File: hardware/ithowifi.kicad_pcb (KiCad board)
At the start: 2 copper layers, 42.3 x 49.5 mm, 8 parts, among them J1 conn

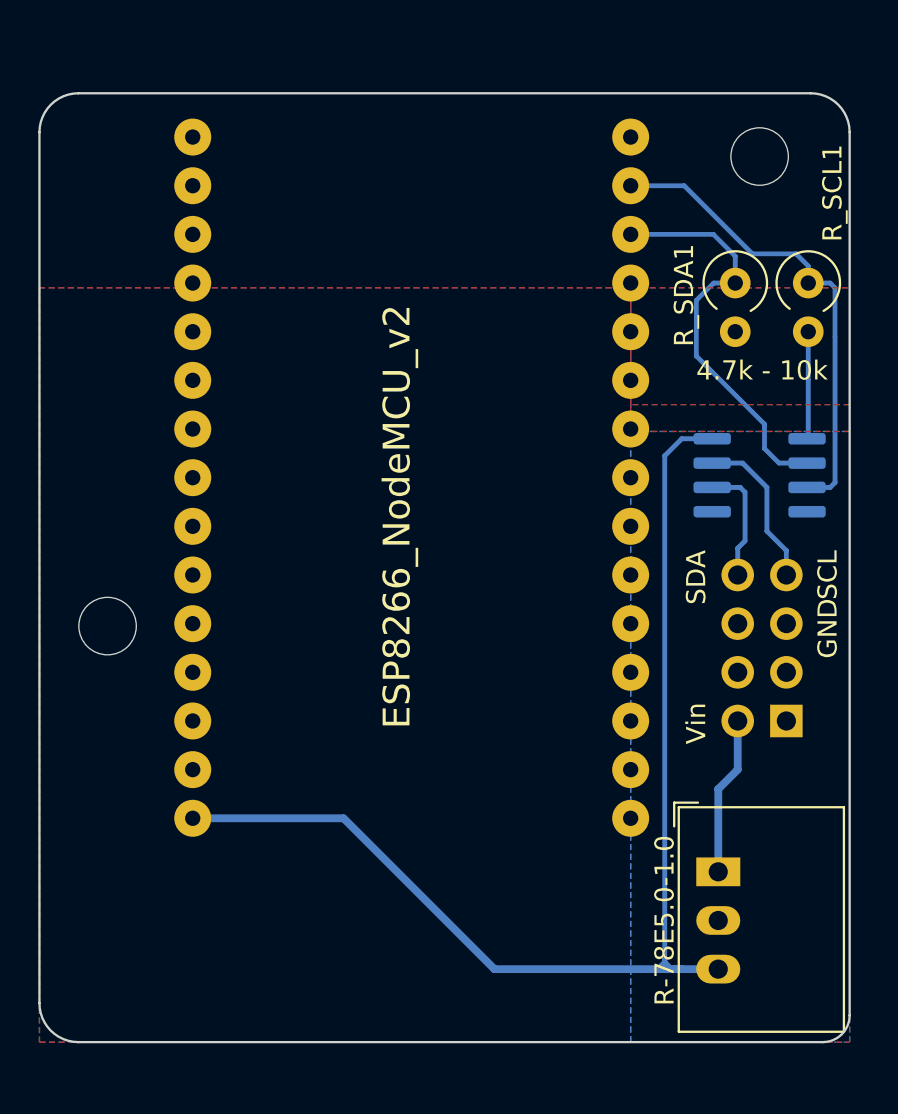
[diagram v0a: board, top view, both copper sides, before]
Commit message: Updated PCB to version 1.1, added more advanced firmware - PCB version 1.0 wasn't working properly, updated version 1.1 is tested and works - Uploaded a more advanced, 'field' configurable firmware and OTA support - Added images of the add-on - Updated readme
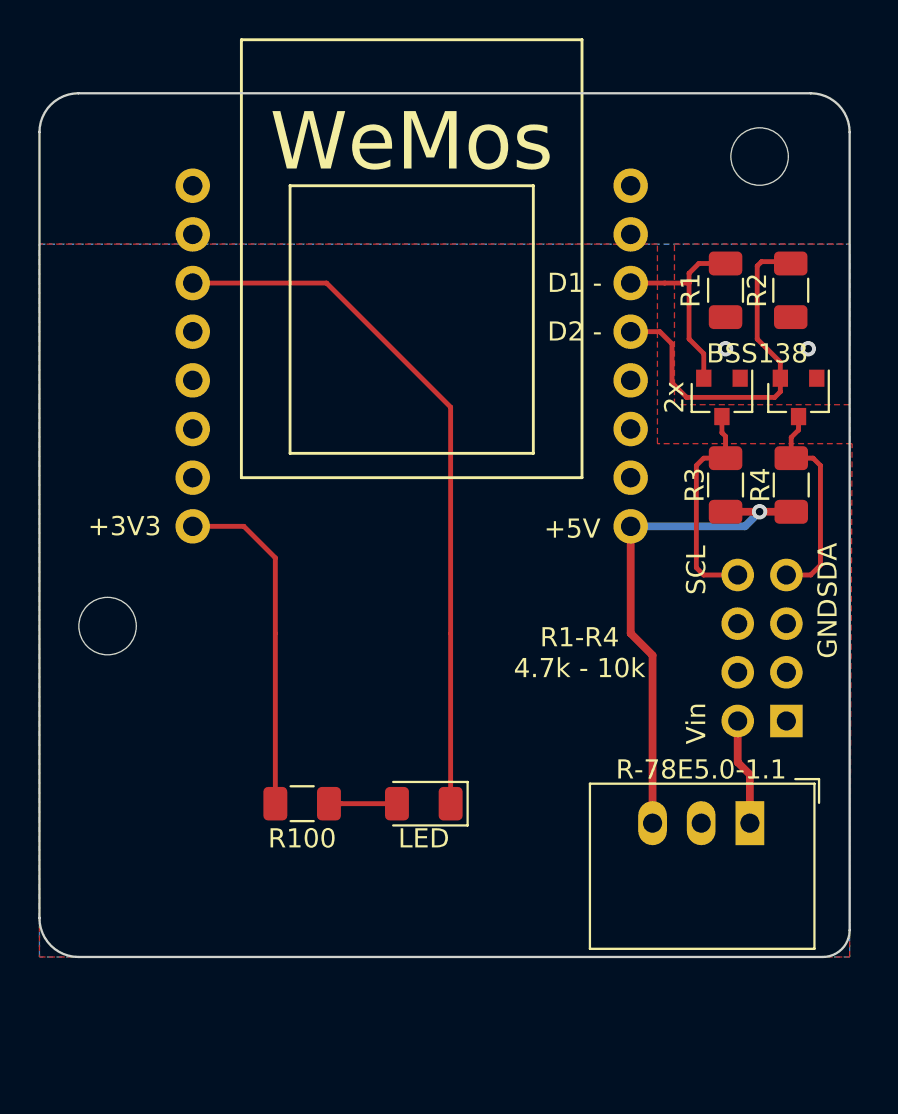
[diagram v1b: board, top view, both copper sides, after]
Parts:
- removed ESP8266_NodeMCU_v2: U1, MCU_NodeMCU:ESP12E_DEVKIT
- removed ISO1540: U3, Package_SO:SOIC-8_3.9x4.9mm_P1.27mm
- removed R-78E5.0-1.0: U2, Converter_DCDC:Converter_DCDC_RECOM_R-78E-0.5_THT
- removed R_SCL1, R_SDA1: R4.7K, Resistor_THT:R_Axial_DIN0309_L9.0mm_D3.2mm_P2.54mm_Vertical
- added 2x: BSS138, Package_TO_SOT_SMD:SOT-23, F.Cu at (118.7, 120.9)
- added BSS138: BSS138, Package_TO_SOT_SMD:SOT-23, F.Cu at (122.7, 120.9)
- added LED: LED, LED_SMD:LED_1206_3216Metric, F.Cu at (103.1, 142.1)
- added R-78E5.0-1.1: U2, Converter_DCDC:Converter_DCDC_RECOM_R-78E-0.5_THT, F.Cu at (120.1, 143.1)
- added R1: R4.7K, Resistor_SMD:R_1206_3216Metric, F.Cu at (118.9, 115.3)
- added R100: R100, Resistor_SMD:R_1206_3216Metric, F.Cu at (96.8, 142.1)
- added R2: R4.7K, Resistor_SMD:R_1206_3216Metric, F.Cu at (122.3, 115.3)
- added R3: R4.7K, Resistor_SMD:R_1206_3216Metric, F.Cu at (118.9, 125.5)
- added R4: R4.7K, Resistor_SMD:R_1206_3216Metric, F.Cu at (122.3, 125.5)
- added U1: WeMos_mini, wemos_d1_mini:D1_mini_board, B.Cu at (102.5, 120.0)
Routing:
- net Net-(D1-Pad1): track 0.00 -> 36.8 mm
- net +5V: track 61.8 -> 26.4 mm, vias 0 -> 1
- net Net-(ESP8266_NodeMCU_v2-PadD1): track 25.1 -> 0.00 mm
- net Net-(ESP8266_NodeMCU_v2-PadD2): track 21.5 -> 0.00 mm
- net Net-(Q1-Pad2): track 0.00 -> 19.5 mm
- net +3V3: track 5.61 -> 17.8 mm, vias 0 -> 2
- net Net-(Q2-Pad2): track 0.00 -> 11.0 mm
- net Net-(J1-Pad8): track 6.42 -> 11.6 mm
- net Net-(D1-Pad2): track 0.00 -> 3.55 mm
- net Net-(J1-Pad7): track 8.50 -> 11.2 mm
- net +16V3: track 8.17 -> 5.60 mm
- net GND: track 0.80 -> 0.00 mm
- removed copper zone on B.Cu, net GND
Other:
- board size 42.3 x 49.5 mm -> 42.3 x 45.1 mm
- board text added: "+3V3"
- board text added: "+5V"
- board text added: "D1 -"
- board text added: "D2 -"
- board text added: "Itho CVE ESP WiFi Controller v1.1 Arjen Hiemstra GNU General Public License 3.0 github.com/arjenhiemstra/ithowifi"
- board text added: "R1-R4 4.7k - 10k"
- board text removed: "4.7k - 10k"
- board text removed: "Itho CVE ESP WiFi Controller v1.0 Arjen Hiemstra GNU General Public License 3.0 github.com/arjenhiemstra/ithowifi"

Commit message: Release 1.2
- Updated PCB design to accommodate a ATTiny 1614 to handle the I2C init with the itho box (Wemos often boots too slow to handle this reliable)
- Added firmware for the ATTiny
- Updated Wemos and basic firmware to work with the ATTiny 1614
- Improved WiFi stability
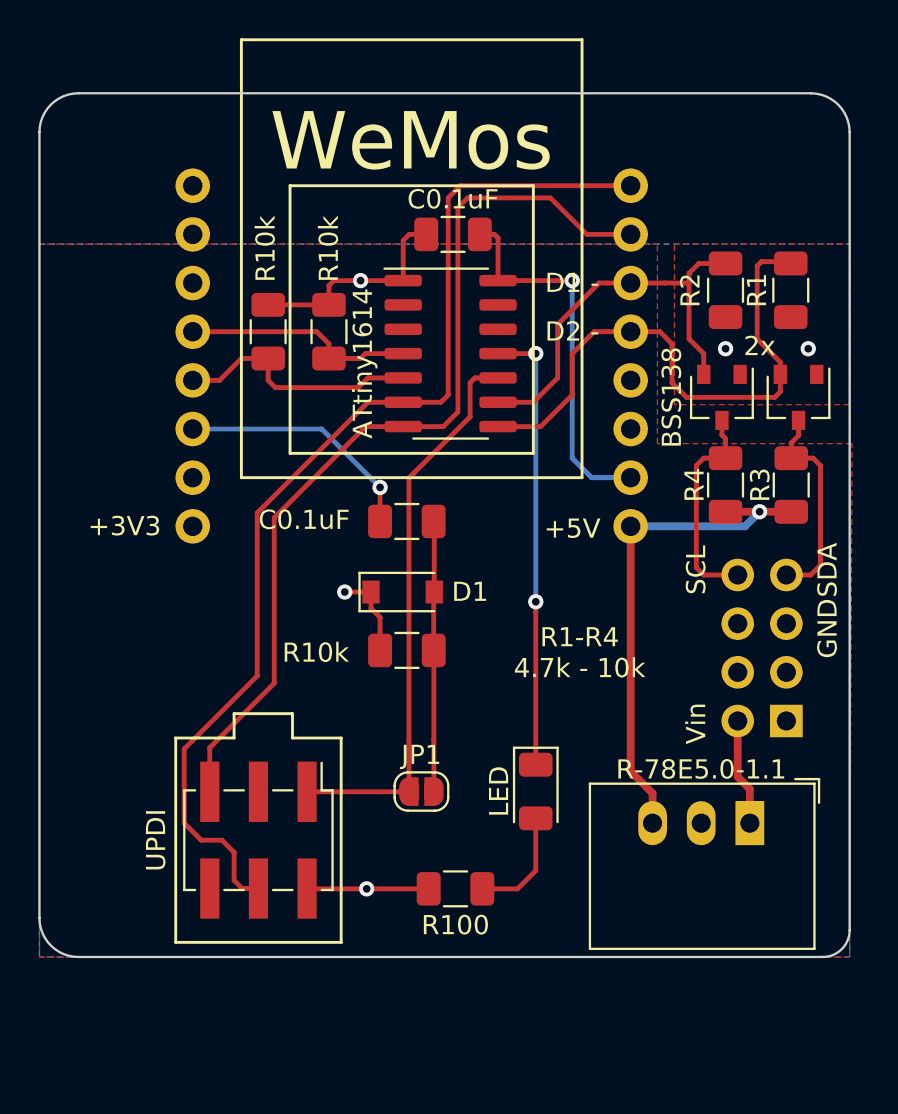
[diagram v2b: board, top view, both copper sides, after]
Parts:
- removed  : 3mm, MountingHole:MountingHole_3mm (x2)
- added ATtiny1614: ATtiny1614-SS, Package_SO:SOIC-14_3.9x8.7mm_P1.27mm, F.Cu at (104.5, 118.6)
- added C0.1uF: 0.1uF, Inductor_SMD:L_1206_3216Metric, F.Cu at (104.6, 112.4)
- added C0.1uF: C0.1uF, Inductor_SMD:L_1206_3216Metric, F.Cu at (102.2, 127.4)
- added D1: D, Diode_SMD:D_SOD-123, F.Cu at (102.0, 131.1)
- added JP1: SolderJumper_2_Open, Jumper:SolderJumper-2_P1.3mm_Open_RoundedPad1.0x1.5mm, F.Cu at (103.0, 141.5)
- added R10k: R10K, Resistor_SMD:R_1206_3216Metric, F.Cu at (95.0, 117.5)
- added R10k: R10K, Resistor_SMD:R_1206_3216Metric, F.Cu at (98.2, 117.5)
- added R10k: R10K, Resistor_SMD:R_1206_3216Metric, F.Cu at (102.2, 134.1)
- added UPDI: Conn_02x03_Odd_Even, Connector_PinHeader_2.54mm:PinHeader_2x03_P2.54mm_Vertical_SMD, F.Cu at (94.5, 144.0)
- 2x: renamed from BSS138; footprint Package_TO_SOT_SMD:SOT-23 -> Package_TO_SOT_SMD:SOT-23W
- BSS138: renamed from 2x; footprint Package_TO_SOT_SMD:SOT-23 -> Package_TO_SOT_SMD:SOT-23W
- R1: renamed from R2; value R4.7K -> R10K
- R2: renamed from R1; value R4.7K -> R10K
- R3: renamed from R4; value R4.7K -> R10K
- R4: renamed from R3; value R4.7K -> R10K
- moved R100 9.16 mm to (104.8, 146.6), turned to 0 degrees
- moved LED 5.88 mm to (109.0, 141.5), turned to 270 degrees
- renumbered J1 to J2
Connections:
- net Net-(J1-Pad7) renamed SDA
- net Net-(J1-Pad8) renamed SCL
- LED pad 1: Net-(D1-Pad1) -> Net-(ATtiny1614-Pad11)
- LED pad 2: Net-(D1-Pad2) -> Net-(R100-Pad2)
- R100 pad 1: Net-(D1-Pad2) -> +3V3
- R100 pad 2: +3V3 -> Net-(R100-Pad2)
- U1 pad 11: Net-(D1-Pad1) -> Net-(U1-Pad11)
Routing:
- net Net-(ATtiny1614-Pad6): track 0.00 -> 56.5 mm
- net Net-(ATtiny1614-Pad7): track 0.00 -> 48.3 mm
- net Net-(D1-Pad1): track 36.8 -> 0.00 mm
- net Net-(ATtiny1614-Pad10): track 0.00 -> 29.9 mm
- net Net-(ATtiny1614-Pad11): track 0.00 -> 23.4 mm, vias 0 -> 2
- net GND: track 0.00 -> 19.9 mm, vias 0 -> 1
- net Net-(C0.1uF1-Pad2): track 0.00 -> 14.1 mm
- net Net-(ATtiny1614-Pad5): track 0.00 -> 13.0 mm
- net Net-(C0.1uF1-Pad1): track 0.00 -> 12.8 mm, vias 0 -> 1
- net Net-(ATtiny1614-Pad4): track 0.00 -> 12.1 mm
- net Net-(ATtiny1614-Pad9): track 11.0 -> 22.1 mm
- net Net-(ATtiny1614-Pad8): track 19.5 -> 29.7 mm
- net Net-(R100-Pad2): track 0.00 -> 5.91 mm
- net +3V3: track 17.8 -> 22.6 mm, vias 2 -> 5
- net Net-(D1-Pad2): track 3.55 -> 0.00 mm
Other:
- board text added: "Itho CVE ESP WiFi Controller v1.2 Arjen Hiemstra GNU General Public License 3.0 github.com/arjenhiemstra/ithowifi"
- board text removed: "Itho CVE ESP WiFi Controller v1.1 Arjen Hiemstra GNU General Public License 3.0 github.com/arjenhiemstra/ithowifi"

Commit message: Version 2.0.3
- Support for hardware revision 2
- Experimental itho RF remote support
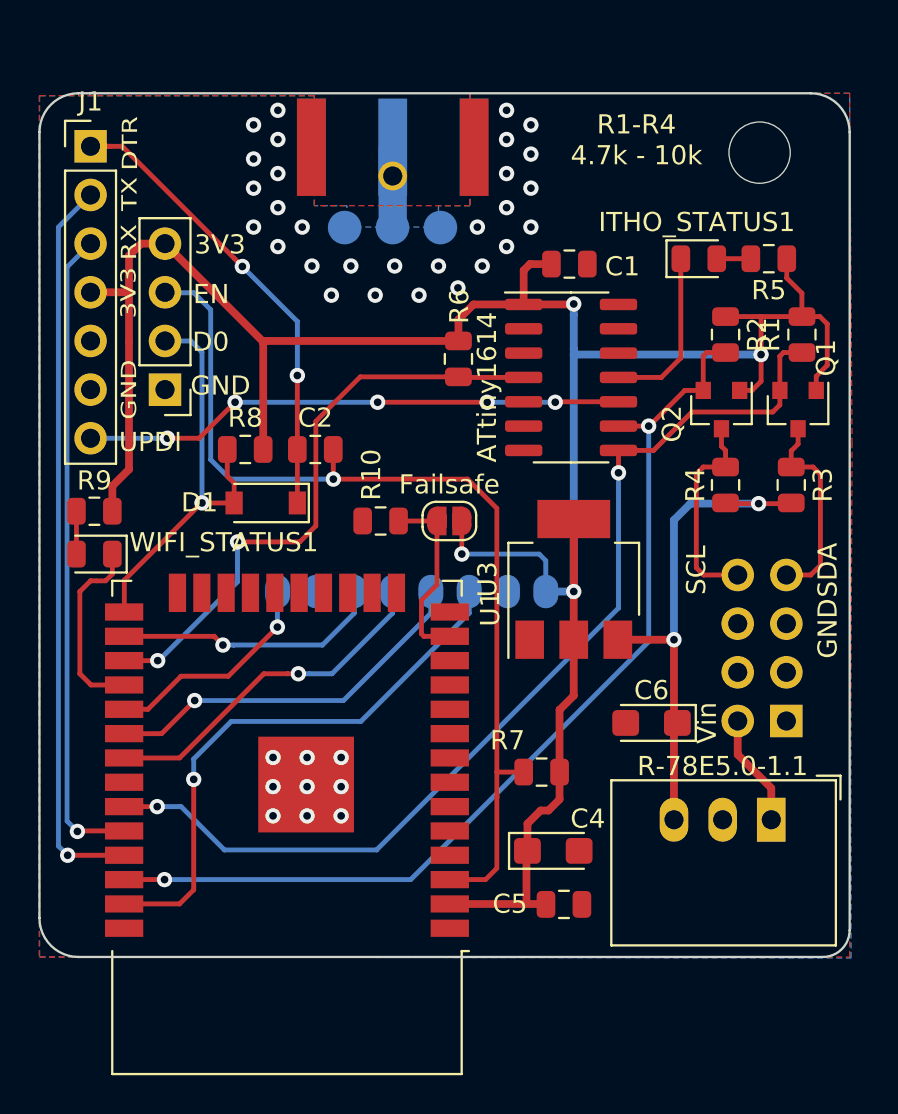
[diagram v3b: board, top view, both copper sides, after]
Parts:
- removed C0.1uF: 0.1uF, Inductor_SMD:L_1206_3216Metric
- removed C0.1uF: C0.1uF, Inductor_SMD:L_1206_3216Metric
- removed LED: LED, LED_SMD:LED_1206_3216Metric
- removed R10k (x3): R10K, Resistor_SMD:R_1206_3216Metric
- removed UPDI: Conn_02x03_Odd_Even, Connector_PinHeader_2.54mm:PinHeader_2x03_P2.54mm_Vertical_SMD
- added C1: 0,1uF, Inductor_SMD:L_0805_2012Metric, F.Cu at (110.7, 113.9)
- added C2: 1uF, Capacitor_SMD:C_0805_2012Metric, F.Cu at (97.5, 123.6)
- added C4: 10uF, Capacitor_Tantalum_SMD:CP_EIA-3216-12_Kemet-S, F.Cu at (109.9, 144.6)
- added C5: 0.1uF, Capacitor_SMD:C_0805_2012Metric, F.Cu at (110.4, 147.4)
- added C6: 10uF, Capacitor_Tantalum_SMD:CP_EIA-3216-12_Kemet-S, F.Cu at (115.0, 137.9)
- added H1: MountingHole, MountingHole:MountingHole_2.5mm, F.Cu at (120.7, 108.1)
- added ITHO_STATUS1: LED, LED_SMD:LED_0805_2012Metric, F.Cu at (117.5, 113.7)
- added J1: CONN_01X07, Connector_PinHeader_2.54mm:PinHeader_1x07_P2.54mm_Vertical, F.Cu at (85.7, 107.8)
- added J3: Conn_Coaxial, Connector_Coaxial:SMA_Amphenol_132289_EdgeMount, B.Cu at (101.5, 107.8)
- added J4: Conn_01x04, Connector_PinHeader_2.54mm:PinHeader_1x04_P2.54mm_Vertical, F.Cu at (89.6, 120.5)
- added R10: 10K, Resistor_SMD:R_0805_2012Metric, F.Cu at (100.9, 127.4)
- added R6: R10K, Resistor_SMD:R_0805_2012Metric, F.Cu at (104.9, 118.9)
- added R7: 10K, Resistor_SMD:R_0805_2012Metric, F.Cu at (109.3, 140.5)
- added R8: 10K, Resistor_SMD:R_0805_2012Metric, F.Cu at (93.8, 123.6)
- added R9: R100, Resistor_SMD:R_0805_2012Metric, F.Cu at (85.9, 126.8)
- added REF**: Pin_D1.0mm_L10.0mm, Connector_Pin:Pin_D1.0mm_L10.0mm, F.Cu at (101.5, 109.3)
- added U2: CC1101-868MHz-Module, nrg_watch:CC1101-868MHz-Module, B.Cu at (102.5, 121.5)
- added U3: AMS1117-3.3, Package_TO_SOT_SMD:SOT-223-3_TabPin2, F.Cu at (110.9, 130.4)
- added WIFI_STATUS1: LED, LED_SMD:LED_0805_2012Metric, F.Cu at (85.9, 129.1)
- D1: value D -> D_Zener
- JP1: value SolderJumper_2_Open -> Failsafe
- Q1: renamed from 2x; footprint Package_TO_SOT_SMD:SOT-23W -> Package_TO_SOT_SMD:SOT-23
- Q2: renamed from BSS138; footprint Package_TO_SOT_SMD:SOT-23W -> Package_TO_SOT_SMD:SOT-23
- R1, R2, R3, R4: footprint Resistor_SMD:R_1206_3216Metric -> Resistor_SMD:R_0805_2012Metric
- R5: renamed from R100; footprint Resistor_SMD:R_1206_3216Metric -> Resistor_SMD:R_0805_2012Metric
- U1: value WeMos_mini -> ESP32-WROOM; footprint wemos_d1_mini:D1_mini_board -> RF_Module:ESP32-WROOM-32; moved to F.Cu
- moved R5 36.7 mm to (121.1, 113.7), turned to 180 degrees
- moved U1 21.4 mm to (96.0, 140.4)
- moved JP1 14.2 mm to (104.5, 127.4)
- moved D1 8.52 mm to (94.9, 126.4), turned to 180 degrees
- moved ATtiny1614 6.41 mm to (110.8, 119.9)
- moved R1 2.38 mm to (122.9, 117.6), turned to 90 degrees
- moved R2 2.31 mm to (118.9, 117.6), turned to 270 degrees
- moved R-78E5.0-1.1 1.13 mm to (121.3, 143.0)
- moved Q1 0.64 mm to (122.7, 121.5)
- moved Q2 0.64 mm to (118.7, 121.5)
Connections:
- ATtiny1614 pad 10: Net-(ATtiny1614-Pad10) -> UPDI
- D1 pad 1: +3V3 -> Net-(C2-Pad2)
- D1 pad 2: Net-(C0.1uF1-Pad2) -> D0
- JP1 pad 1: Net-(C0.1uF1-Pad2) -> +3V3
- JP1 pad 2: Net-(ATtiny1614-Pad10) -> Net-(JP1-Pad2)
- U1 pad 1: +5V -> GND
- U1 pad 12: Net-(ATtiny1614-Pad4) -> Net-(U1-Pad12)
- U1 pad 13: Net-(ATtiny1614-Pad5) -> Net-(JP1-Pad2)
- U1 pad 15: Net-(U1-Pad15) -> GND
- U1 pad 16: +3V3 -> Net-(U1-Pad16)
- U1 pad 2: GND -> +3V3
- U1 pad 3: Net-(U1-Pad3) -> EN
- U1 pad 5: Net-(ATtiny1614-Pad8) -> Net-(U1-Pad5)
- U1 pad 6: Net-(ATtiny1614-Pad9) -> Net-(U1-Pad6)
- U1 pad 7: Net-(ATtiny1614-Pad7) -> Net-(U1-Pad7)
- U1 pad 8: Net-(ATtiny1614-Pad6) -> Net-(U1-Pad8)
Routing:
- net +3V3: track 22.6 -> 129.6 mm, vias 5 -> 4
- net Net-(ATtiny1614-Pad6): track 56.5 -> 0.00 mm
- net EN: track 0.00 -> 51.1 mm, vias 0 -> 1
- net Net-(ATtiny1614-Pad7): track 48.3 -> 0.00 mm
- net D1/TX0: track 0.00 -> 38.3 mm, vias 0 -> 1
- net D0/RX0: track 0.00 -> 34.1 mm, vias 0 -> 1
- net Net-(ATtiny1614-Pad9): track 22.1 -> 52.0 mm, vias 0 -> 2
- net Net-(ATtiny1614-Pad10): track 29.9 -> 0.00 mm
- net D23_MOSI: track 0.00 -> 29.4 mm, vias 0 -> 1
- net UPDI: track 0.00 -> 28.3 mm, vias 0 -> 5
- net Net-(C2-Pad2): track 0.00 -> 25.2 mm, vias 0 -> 2
- net Net-(ATtiny1614-Pad8): track 29.7 -> 53.4 mm, vias 0 -> 2
- net D0: track 0.00 -> 22.1 mm, vias 0 -> 1
- net GND: track 19.9 -> 0.00 mm, vias 1 -> 38
- net D18_SCK: track 0.00 -> 19.7 mm, vias 0 -> 1
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- added copper zone on B.Cu, net GND
- removed copper zone on B.Cu, net +3V3
- removed copper zone on F.Cu, net +3V3
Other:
- board text added: "3V3"
- board text added: "D0"
- board text added: "DTR"
- board text added: "EN"
- board text added: "Itho CVE ESP WiFi Controller v2.2 Arjen Hiemstra - GNU GPL 3.0"
- board text added: "RX"
- board text added: "TX"
- board text added: "UPDI"
- board text added: "https://github.com/arjenhiemstra/ithowifi"
- board text removed: "+3V3"
- board text removed: "+5V"
- board text removed: "D1 -"
- board text removed: "D2 -"
- board text removed: "Itho CVE ESP WiFi Controller v1.2 Arjen Hiemstra GNU General Public License 3.0 github.com/arjenhiemstra/ithowifi"
